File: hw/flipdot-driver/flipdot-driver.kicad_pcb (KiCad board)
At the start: 2 copper layers, 67.5 x 49.5 mm, 93 parts, among them J1 DISPLAY, J2 NRF_CON, J3 Prog, J4 I2C, J5 USART, J6 USB, J7 USB_B_Micro, J8 RST, J9 MAIN_Power, Q1 MMBTA64, Q10 MMBTA64, Q11 MMBTA64, Q12 MMBTA64, Q13 MMBTA64, Q14 MMBTA64, Q15 Q_NMOS_GSD, Q16 Q_NMOS_GSD, Q17 Q_NMOS_GSD, Q18 Q_NMOS_GSD, Q2 MMBTA64, Q3 MMBTA64, Q4 MMBTA64, Q5 MMBTA64, Q6 MMBTA64, Q7 MMBTA64, Q8 MMBTA64, Q9 MMBTA64, U1 AT25xxx, U2 ULN2003A, U3 USBLC6-2SC6, U4 AZ1117-3.3, U5 ULN2003A, U6 stm32_STM32F103C(8-B)Tx, U7 74HC595, U8 AX5201, U9 74HC595, Y1 32768, Y2 8MHz/20pF

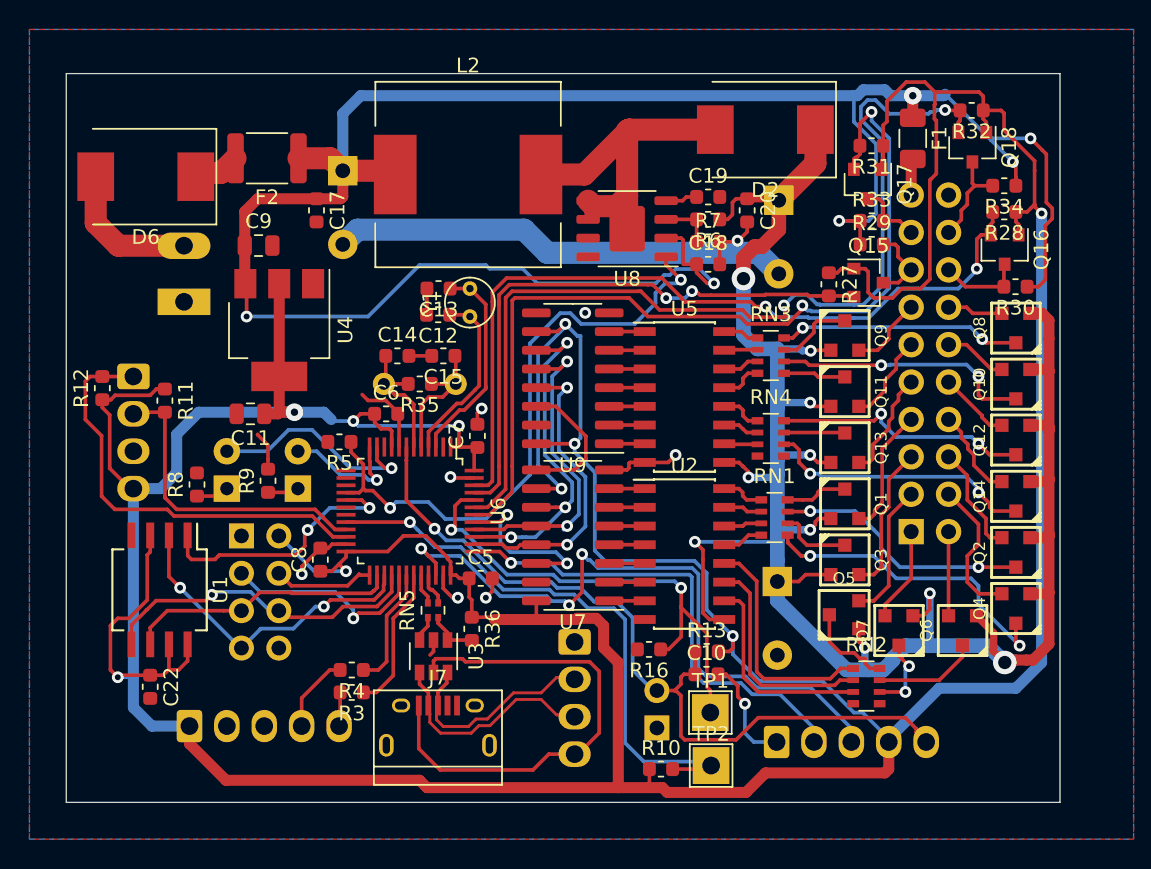
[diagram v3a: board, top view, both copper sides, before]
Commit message: Placed labels, NRF connector mirrored.
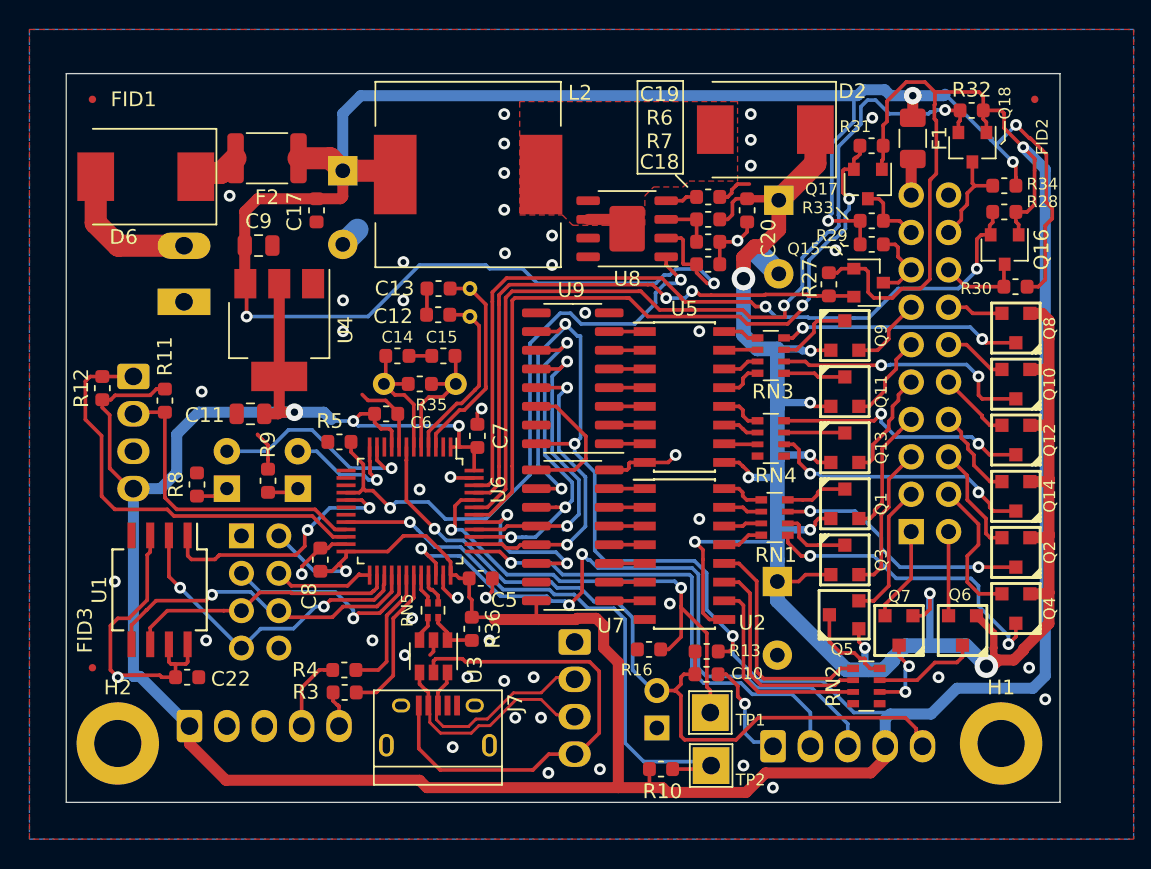
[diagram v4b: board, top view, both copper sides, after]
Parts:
- added FID1: Fiducial_0.5mm_Mask1.5mm, Fiducial:Fiducial_0.5mm_Mask1.5mm, F.Cu at (139.2, 27.4)
- added FID2: Fiducial_0.5mm_Mask1.5mm, Fiducial:Fiducial_0.5mm_Mask1.5mm, F.Cu at (203.2, 27.4)
- added FID3: Fiducial_0.5mm_Mask1.5mm, Fiducial:Fiducial_0.5mm_Mask1.5mm, F.Cu at (139.2, 66.0)
- added H1: MountingHole_Pad, MountingHole:MountingHole_3.2mm_M3_DIN965_Pad, F.Cu at (200.9, 71.2)
- added H2: MountingHole_Pad, MountingHole:MountingHole_3.2mm_M3_DIN965_Pad, F.Cu at (140.9, 71.2)
- Y1: moved to B.Cu
- moved C22 2.59 mm to (145.6, 66.7), turned to 0 degrees
- moved R4 0.51 mm to (156.3, 66.2)
- moved R3 0.48 mm to (156.3, 67.7)
- moved J3 0.38 mm to (185.4, 71.3)
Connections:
- J2 pad 8: /NRF_IRQ -> (no net)
- J5 pad 2: Net-(J5-Pad2) -> (no net)
- J7 pad 4: Net-(J7-Pad4) -> (no net)
- RN2 pad 4: Net-(RN2-Pad4) -> (no net)
- RN2 pad 5: Net-(RN2-Pad5) -> (no net)
- RN4 pad 4: Net-(RN4-Pad4) -> (no net)
- RN4 pad 5: Net-(RN4-Pad5) -> (no net)
- U6 pad 10: Net-(U6-Pad10) -> (no net)
- U6 pad 13: Net-(U6-Pad13) -> (no net)
- U6 pad 14: Net-(U6-Pad14) -> (no net)
- U6 pad 15: Net-(U6-Pad15) -> (no net)
- U6 pad 18: Net-(U6-Pad18) -> (no net)
- U6 pad 19: Net-(U6-Pad19) -> (no net)
- U6 pad 2: Net-(U6-Pad2) -> (no net)
- U7 pad 15: Net-(U7-Pad15) -> (no net)
- U9 pad 15: Net-(U9-Pad15) -> (no net)
- U9 pad 9: Net-(U9-Pad9) -> (no net)
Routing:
- net GND: track 71.6 -> 46.3 mm, vias 9 -> 50
- net Net-(D2-Pad2): track 24.0 -> 2.91 mm
- net /LV_RST: track 61.1 -> 50.8 mm
- net /LV_CLK: track 66.0 -> 61.2 mm
- net +3V3: track 355.6 -> 360.1 mm
- net /SWCLK: track 32.0 -> 33.4 mm
- net /SWDIO: track 44.9 -> 45.8 mm
- net +24V: track 143.5 -> 142.6 mm
- net +12V: track 147.7 -> 147.0 mm
- net /USART_TX: track 8.25 -> 8.76 mm
- added copper zone on F.Cu, net Net-(D2-Pad2)
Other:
- board text added: "+"
- board text added: "-"
- board text added: "12V IN"
- board text added: "Flipdot display driver Jethro, 2019 v0.1"
- board text added: "I2C"
- board text added: "SDA SCL GND +3V3"

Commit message: Forgotten labes.
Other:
- board text added: "+3V3"
- board text added: "BOOT0"
- board text added: "BOOT1"
- board text added: "D+"
- board text added: "D-"
- board text added: "DISPLAY"
- board text added: "GND"
- board text added: "GND SWCLK SWDIO +3V3 NRST"
- board text added: "LED1"
- board text added: "LED2"
- board text added: "NC"
- board text added: "NRF"
- board text added: "PROG"
- board text added: "RST"
- board text added: "RX"
- board text added: "TX"
- board text added: "UART"
- board text added: "USB"
- board text added: "VBUS"
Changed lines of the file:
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@@
   (general
     (thickness 1.6)
-    (drawings 31)
+    (drawings 67)
     (tracks 1413)
     (zones 0)
@@
     (descr "Through hole straight IDC box header, 2x10, 2.54mm pitch, double rows")
     (tags "Through hole IDC box header THT 2x10 2.54mm double row")
-    (fp_text reference J1 (at 1.27 6.604) (layer B.SilkS)
+    (fp_text reference J1 (at 7.124 4.927) (layer B.SilkS)
       (effects (font (size 1 1) (thickness 0.15)) (justify mirror))
     )
@@
     (descr "Molex KK-254 Interconnect System, old/engineering part number: AE-6410-05A example for new part number: 22-27-2051, 5 Pins (http://www.molex.com/pdm_docs/sd/022272021_sd.pdf), generated with kicad-footprint-generator")
     (tags "connector Molex KK-254 side entry")
-    (fp_text reference J5 (at 5.08 4.12) (layer B.SilkS)
+    (fp_text reference J5 (at 12.966 -2.947) (layer B.SilkS)
       (effects (font (size 1 1) (thickness 0.15)) (justify mirror))
     )
@@
     (descr "Molex KK-254 Interconnect System, old/engineering part number: AE-6410-04A example for new part number: 22-27-2041, 4 Pins (http://www.molex.com/pdm_docs/sd/022272021_sd.pdf), generated with kicad-footprint-generator")
     (tags "connector Molex KK-254 side entry")
-    (fp_text reference J6 (at 3.81 4.12 270) (layer B.SilkS)
+    (fp_text reference J6 (at 9.88 -2.552) (layer B.SilkS)
       (effects (font (size 1 1) (thickness 0.15)) (justify mirror))
     )
@@
     (descr "Through hole straight socket strip, 1x02, 2.54mm pitch, single row (from Kicad 4.0.7), script generated")
     (tags "Through hole socket strip THT 1x02 2.54mm single row")
-    (fp_text reference J8 (at 0 2.77) (layer B.SilkS)
+    (fp_text reference J8 (at -1.258 2.514) (layer B.SilkS)
       (effects (font (size 1 1) (thickness 0.15)) (justify mirror))
     )
@@
     (descr "LED, diameter 3.0mm, 2 pins")
     (tags "LED diameter 3.0mm 2 pins")
-    (fp_text reference D7 (at 4.598 1.282) (layer B.SilkS)
+    (fp_text reference D7 (at -2.26 -1.512 90) (layer B.SilkS)
       (effects (font (size 1 1) (thickness 0.15)) (justify mirror))
     )
@@
     (descr "LED, diameter 3.0mm, 2 pins")
     (tags "LED diameter 3.0mm 2 pins")
-    (fp_text reference D8 (at 4.49 1.264) (layer B.SilkS)
+    (fp_text reference D8 (at -2.26 1.79 90) (layer B.SilkS)
       (effects (font (size 1 1) (thickness 0.15)) (justify mirror))
     )
@@
     (descr "CP, Radial series, Radial, pin pitch=5.00mm, , diameter=10mm, Electrolytic Capacitor")
     (tags "CP Radial series Radial pin pitch 5.00mm  diameter 10mm Electrolytic Capacitor")
-    (fp_text reference C23 (at 2.5 6.25 90) (layer B.SilkS)
+    (fp_text reference C23 (at 4.332 -6.056 90) (layer B.SilkS)
       (effects (font (size 1 1) (thickness 0.15)) (justify mirror))
     )
@@
       (net 2 GND))
   )
+  (gr_text NRF (at 146.316 65.506) (layer B.SilkS)
+    (effects (font (size 1 1) (thickness 0.15)) (justify mirror))
+  )
+  (gr_line (start 180.098 58.394) (end 180.098 51.79) (layer B.SilkS) (width 0.12))
+  (gr_line (start 172.732 58.394) (end 180.098 58.394) (layer B.SilkS) (width 0.12))
+  (gr_line (start 172.732 57.886) (end 172.732 58.394) (layer B.SilkS) (width 0.12))
+  (gr_line (start 172.732 51.79) (end 172.732 57.886) (layer B.SilkS) (width 0.12))
+  (gr_line (start 180.098 51.79) (end 172.732 51.79) (layer B.SilkS) (width 0.12))
+  (gr_circle (center 196.458 67.792) (end 196.608 67.792) (layer B.SilkS) (width 0.25))
+  (gr_circle (center 179.336 53.822) (end 179.486 53.822) (layer B.SilkS) (width 0.25))
+  (gr_line (start 179.336 53.822) (end 173.24 53.822) (layer B.SilkS) (width 0.12))
+  (gr_line (start 196.608 67.792) (end 187.718 67.792) (layer B.SilkS) (width 0.12))
+  (gr_text PROG (at 176.034 52.806) (layer B.SilkS)
+    (effects (font (size 1 1) (thickness 0.15)) (justify mirror))
+  )
+  (gr_text PROG (at 191.274 67.03) (layer B.SilkS)
+    (effects (font (size 1 1) (thickness 0.15)) (justify mirror))
+  )
+  (gr_text "GND\nSWCLK\nSWDIO\n+3V3\nNRST" (at 176.288 54.076 90) (layer B.SilkS)
+    (effects (font (size 0.8 0.8) (thickness 0.15)) (justify left mirror))
+  )
+  (gr_text DISPLAY (at 201.688 45.44 90) (layer B.SilkS)
+    (effects (font (size 1 1) (thickness 0.15)) (justify mirror))
+  )
+  (gr_line (start 177.558 65.506) (end 177.558 66.014) (layer B.SilkS) (width 0.12))
+  (gr_line (start 179.082 65.252) (end 179.082 62.204) (layer B.SilkS) (width 0.12))
+  (gr_line (start 176.288 65.252) (end 179.082 65.252) (layer B.SilkS) (width 0.12))
+  (gr_line (start 176.288 62.204) (end 176.288 65.252) (layer B.SilkS) (width 0.12))
+  (gr_line (start 179.082 62.204) (end 176.288 62.204) (layer B.SilkS) (width 0.12))
+  (gr_text BOOT0 (at 180.098 65.76 90) (layer B.SilkS)
+    (effects (font (size 0.8 0.8) (thickness 0.15)) (justify mirror))
+  )
+  (gr_text BOOT1 (at 177.812 73.888) (layer B.SilkS)
+    (effects (font (size 0.8 0.8) (thickness 0.15)) (justify mirror))
+  )
+  (gr_text GND (at 178.828 64.49) (layer B.SilkS)
+    (effects (font (size 0.8 0.8) (thickness 0.15)) (justify left mirror))
+  )
+  (gr_text RST (at 178.828 63.22) (layer B.SilkS)
+    (effects (font (size 0.8 0.8) (thickness 0.15)) (justify left mirror))
+  )
+  (gr_text VBUS (at 168.16 71.856 90) (layer B.SilkS)
+    (effects (font (size 0.8 0.8) (thickness 0.15)) (justify mirror))
+  )
+  (gr_text D- (at 167.144 69.316 90) (layer B.SilkS)
+    (effects (font (size 0.8 0.8) (thickness 0.15)) (justify mirror))
+  )
+  (gr_text D+ (at 168.16 66.776 90) (layer B.SilkS)
+    (effects (font (size 0.8 0.8) (thickness 0.15)) (justify mirror))
+  )
+  (gr_text GND (at 168.16 64.236 90) (layer B.SilkS)
+    (effects (font (size 0.8 0.8) (thickness 0.15)) (justify mirror))
+  )
+  (gr_text USB (at 170.192 74.142) (layer B.SilkS)
+    (effects (font (size 1 1) (thickness 0.15)) (justify mirror))
+  )
+  (gr_text +3V3 (at 145.808 73.888) (layer B.SilkS)
+    (effects (font (size 0.8 0.8) (thickness 0.15)) (justify mirror))
+  )
+  (gr_text NC (at 148.348 73.888) (layer B.SilkS)
+    (effects (font (size 0.8 0.8) (thickness 0.15)) (justify mirror))
+  )
+  (gr_text GND (at 150.888 73.888) (layer B.SilkS)
+    (effects (font (size 0.8 0.8) (thickness 0.15)) (justify mirror))
+  )
+  (gr_text TX (at 153.428 73.888) (layer B.SilkS)
+    (effects (font (size 0.8 0.8) (thickness 0.15)) (justify mirror))
+  )
+  (gr_text RX (at 155.968 73.888) (layer B.SilkS)
+    (effects (font (size 0.8 0.8) (thickness 0.15)) (justify mirror))
+  )
+  (gr_text UART (at 159.778 73.38) (layer B.SilkS)
+    (effects (font (size 1 1) (thickness 0.15)) (justify mirror))
+  )
+  (gr_text LED2 (at 152.92 49.504) (layer B.SilkS)
+    (effects (font (size 1 1) (thickness 0.15)) (justify mirror))
+  )
+  (gr_text LED1 (at 148.094 49.504) (layer B.SilkS)
+    (effects (font (size 1 1) (thickness 0.15)) (justify mirror))
+  )
   (gr_circle (center 145.808 44.678) (end 145.958 44.678) (layer B.SilkS) (width 0.25))

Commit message: Ready for manufacturing.
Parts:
- FID1, FID2, FID3: value Fiducial_0.5mm_Mask1.5mm -> Fiducial; footprint Fiducial:Fiducial_0.5mm_Mask1.5mm -> Fiducial:Fiducial_0.75mm_Dia_1.5mm_Outer
- moved FID3 37.9 mm to (139.9, 28.2)
- moved FID1 37.8 mm to (138.9, 65.2)
- moved J2 7.80 mm to (151.3, 64.6), turned to 0 degrees
- moved FID2 0.80 mm to (202.9, 28.2)
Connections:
- J2 pad 1: GND -> +3V3
- J2 pad 2: +3V3 -> GND
- J2 pad 3: /NRF_CE -> /NRF_SS
- J2 pad 4: /NRF_SS -> /NRF_CE
- J2 pad 5: /SPI_SCK -> /SPI_MOSI
- J2 pad 6: /SPI_MOSI -> /SPI_SCK
- J2 pad 7: /SPI_MISO -> /NRF_IRQ
- J2 pad 8: (no net) -> /SPI_MISO
- J5 pad 2: (no net) -> Net-(J5-Pad2)
- J7 pad 4: (no net) -> Net-(J7-Pad4)
- RN2 pad 4: (no net) -> Net-(RN2-Pad4)
- RN2 pad 5: (no net) -> Net-(RN2-Pad5)
- RN4 pad 4: (no net) -> Net-(RN4-Pad4)
- RN4 pad 5: (no net) -> Net-(RN4-Pad5)
- U6 pad 10: (no net) -> Net-(U6-Pad10)
- U6 pad 13: (no net) -> Net-(U6-Pad13)
- U6 pad 14: (no net) -> Net-(U6-Pad14)
- U6 pad 15: (no net) -> Net-(U6-Pad15)
- U6 pad 18: (no net) -> Net-(U6-Pad18)
- U6 pad 19: (no net) -> Net-(U6-Pad19)
- U6 pad 2: (no net) -> Net-(U6-Pad2)
- U7 pad 15: (no net) -> Net-(U7-Pad15)
- U9 pad 15: (no net) -> Net-(U9-Pad15)
- U9 pad 9: (no net) -> Net-(U9-Pad9)
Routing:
- net +3V3: track 360.1 -> 364.3 mm, vias 10 -> 9
- net /NRF_SS: track 6.87 -> 9.47 mm, vias 0 -> 1
- net /SPI_MOSI: track 22.5 -> 24.8 mm, vias 1 -> 0
- net /SPI_SCK: track 18.6 -> 19.7 mm, vias 0 -> 1
- net /FLASH_SS: track 17.6 -> 18.1 mm
- net /NRF_CE: track 14.3 -> 14.1 mm, vias 1 -> 0
- net /SPI_MISO: track 22.1 -> 22.0 mm, vias 2 -> 0
- net GND: vias 50 -> 64
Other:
- outline, holes or cut-outs redrawn

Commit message: Better ground planes.
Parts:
- added C2: 47u, Capacitor_THT:CP_Radial_D6.3mm_P2.50mm, B.Cu at (187.2, 47.6)
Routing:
- net /LV_CLK: track 61.2 -> 65.8 mm
- net /24V_EN: track 42.5 -> 40.2 mm
- net +12V: track 147.0 -> 145.1 mm
- net +3V3: track 364.3 -> 366.0 mm
- net +24V: track 142.6 -> 143.3 mm, vias 10 -> 9
- net Net-(RN2-Pad1): track 15.9 -> 16.5 mm
- net Net-(RN2-Pad3): track 14.2 -> 14.8 mm
- net Net-(RN2-Pad2): track 15.0 -> 15.6 mm
- net /LV_RST: track 50.8 -> 51.4 mm
- net GND: vias 64 -> 70
